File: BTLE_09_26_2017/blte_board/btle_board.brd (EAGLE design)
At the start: 45.7 x 43.2 mm, 15 parts, among them P3 USB-B1HSB6, P4 POWER_JACKPTH, P9 44764-1201

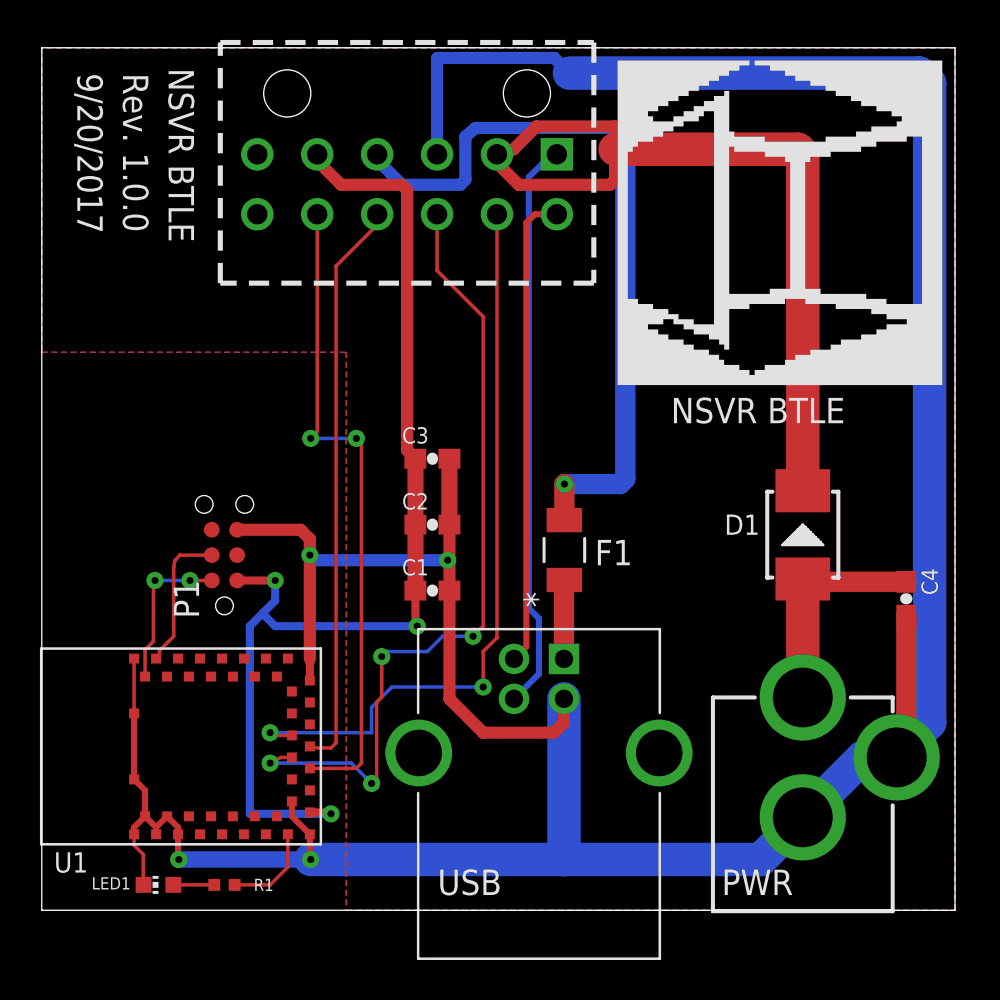
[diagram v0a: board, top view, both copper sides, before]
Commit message: Add Battery & Mounting Holes to BLTE board
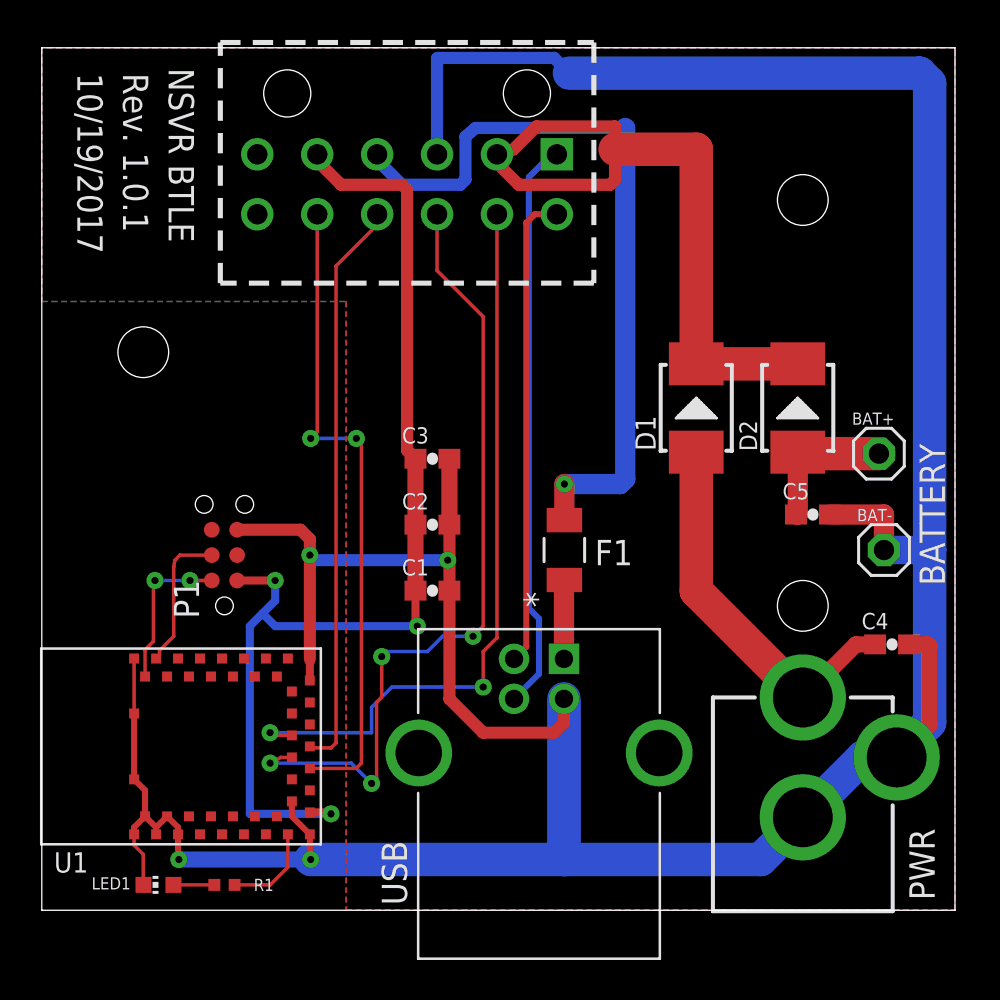
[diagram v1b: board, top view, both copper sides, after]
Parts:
- removed U$4, U$5: (no value), nsvr:NSVR_LOGO
- added BAT+, BAT-: (no value), PatternAgents-ProtoPads:WPAD-1-PTH-2.54
- added C5: 10uF, PatternAgents-ProtoPads:0603-CAP
- added D2: 28V-5A, Seeed-Diode-2016:DO-214AA
- added U$6: (no value), nsvr:NSVR_LOGO
- moved D1 8.29 mm to (32.8, 25.1)
- moved C4 2.39 mm to (42.6, 13.3), turned to 0 degrees
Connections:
- new net VBAT_DC: BAT+.1, C5.1, D2.+
- net GND: now also BAT-.1, C5.2
- net VIN: now also D2.-
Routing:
- net VIN_DC: track 11.2 -> 19.2 mm
- net VBAT_DC: track 0.00 -> 7.35 mm
- net GND: track 175.3 -> 182.1 mm
- net VIN: track 42.3 -> 35.9 mm
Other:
- board text added: "10/19/2017"
- board text added: "BATTERY"
- board text added: "Rev. 1.0.1"
- board text removed: "9/20/2017"
- board text removed: "Rev. 1.0.0"
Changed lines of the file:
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@@
 <wire x1="45.72" y1="43.18" x2="45.72" y2="0" width="0" layer="20"/>
 <wire x1="45.72" y1="0" x2="0" y2="0" width="0" layer="20"/>
-<text x="31.496" y="24.384" size="1.27" layer="21" font="vector" ratio="20">NSVR BTLE</text>
 <text x="6.35" y="42.164" size="1.27" layer="21" font="vector" ratio="20" rot="SR270">NSVR BTLE</text>
-<text x="4.064" y="41.91" size="1.27" layer="21" font="vector" ratio="20" rot="SR270">Rev. 1.0.0</text>
-<text x="1.778" y="41.91" size="1.27" layer="21" font="vector" ratio="20" rot="SR270">9/20/2017</text>
+<text x="4.064" y="41.91" size="1.27" layer="21" font="vector" ratio="20" rot="SR270">Rev. 1.0.1</text>
+<text x="1.778" y="41.91" size="1.27" layer="21" font="vector" ratio="20" rot="SR270">10/19/2017</text>
 <text x="27.686" y="17.272" size="1.27" layer="21" font="vector" ratio="20">F1</text>
-<text x="19.812" y="0.762" size="1.27" layer="21" font="vector" ratio="20">USB</text>
-<text x="34.036" y="0.762" size="1.27" layer="21" font="vector" ratio="20">PWR</text>
+<text x="18.288" y="0.254" size="1.27" layer="21" font="vector" ratio="20" rot="R90">USB</text>
+<text x="44.704" y="0.508" size="1.27" layer="21" font="vector" ratio="20" rot="R90">PWR</text>
+<text x="45.212" y="16.256" size="1.27" layer="21" font="vector" ratio="20" rot="R90">BATTERY</text>
+<hole x="38.1" y="35.56" drill="2.54"/>
+<hole x="5.08" y="27.94" drill="2.54"/>
+<hole x="38.1" y="15.24" drill="2.54"/>
 </plain>
 <attributes>
@@
 <attribute name="PROD_ID" value="CONN-08197" x="78.74" y="-51.308" size="1.778" layer="27" display="off"/>
 </element>
-<element name="C4" library="PatternAgents-ProtoPads" package="0603-CAP" value="10uF" x="43.2816" y="15.5956" rot="R270"/>
+<element name="C4" library="PatternAgents-ProtoPads" package="0603-CAP" value="10uF" x="42.5704" y="13.3096"/>
 <element name="F1" library="1206L050" package="1206LSERIES" value="1206L050YR" x="26.162" y="18.034" smashed="yes" rot="R90">
 <attribute name="COPYRIGHT" value="Copyright C 2015 Accelerated Designs. All rights reserved" x="92.202" y="38.354" size="1.778" layer="27" rot="R90" display="off"/>
@@
 <attribute name="MF" value="On Shore Technology" x="47.752" y="-50.546" size="1.778" layer="27" display="off"/>
 </element>
-<element name="D1" library="Seeed-Diode-2016" package="DO-214AA" value="28V-5A" x="38.1" y="18.796" smashed="yes" rot="R90">
-<attribute name="MPN" value="SS54B" x="38.1" y="18.796" size="1.778" layer="27" rot="R90" display="off"/>
-<attribute name="NAME" x="35.941" y="19.812" size="1.016" layer="25" font="vector" ratio="20" rot="R180"/>
-<attribute name="VALUE" x="40.894" y="17.145" size="0.635" layer="27" ratio="10" rot="R90"/>
-<attribute name="NAME" x="38.1" y="20.066" size="0.5" layer="33" ratio="10" rot="R270"/>
+<element name="D1" library="Seeed-Diode-2016" package="DO-214AA" value="28V-5A" x="32.766" y="25.146" smashed="yes" rot="R90">
+<attribute name="MPN" value="SS54B" x="32.766" y="25.146" size="1.778" layer="27" rot="R90" display="off"/>
+<attribute name="NAME" x="29.718" y="24.765" size="1.016" layer="25" font="vector" ratio="20" rot="R270"/>
+<attribute name="VALUE" x="35.56" y="23.495" size="0.635" layer="27" ratio="10" rot="R90"/>
+<attribute name="NAME" x="32.766" y="26.416" size="0.5" layer="33" ratio="10" rot="R270"/>
 </element>
 <element name="C3" library="PatternAgents-ProtoPads" package="0603-CAP" value="10uF" x="19.558" y="22.606"/>
@@
 <attribute name="NAME" x="10.61" y="1.27" size="0.6096" layer="25" font="vector" ratio="20" align="center-left"/>
 </element>
-<element name="U$4" library="nsvr" package="NSVR_LOGO" value="" x="28.956" y="26.416"/>
-<element name="U$5" library="nsvr" package="NSVR_LOGO" value="" x="44.958" y="26.416" rot="MR0"/>
+<element name="C5" library="PatternAgents-ProtoPads" package="0603-CAP" value="10uF" x="38.608" y="19.812"/>
+<element name="D2" library="Seeed-Diode-2016" package="DO-214AA" value="28V-5A" x="37.846" y="25.146" rot="R90">
+<attribute name="MPN" value="SS54B" x="41.656" y="25.146" size="1.778" layer="27" rot="R90" display="off"/>
+</element>
+<element name="BAT+" library="PatternAgents-ProtoPads" package="WPAD-1-PTH-2.54" value="" x="41.91" y="22.86">
+<attribute name="BOM" value="EXCLUDE" x="41.91" y="22.86" size="1.27" layer="27" ratio="20" display="off"/>
+</element>
+<element name="BAT-" library="PatternAgents-ProtoPads" package="WPAD-1-PTH-2.54" value="" x="42.164" y="18.034">
+<attribute name="BOM" value="EXCLUDE" x="42.164" y="18.034" size="1.27" layer="27" ratio="20" display="off"/>
+</element>
+<element name="U$6" library="nsvr" package="NSVR_LOGO" value="" x="44.958" y="26.67" rot="MR0"/>
 </elements>
 <signals>
@@
 <vertex x="45.72" y="43.18"/>
 <vertex x="0" y="43.18"/>
-<vertex x="0" y="27.94"/>
-<vertex x="15.24" y="27.94"/>
+<vertex x="0" y="30.48"/>
+<vertex x="15.24" y="30.48"/>
 </polygon>
 <polygon width="0.254" layer="16" spacing="0.254" pour="hatch" isolate="0.254" orphans="yes">
@@
 <vertex x="45.72" y="43.18"/>
 <vertex x="0" y="43.18"/>
-<vertex x="0" y="27.94"/>
-<vertex x="15.24" y="27.94"/>
+<vertex x="0" y="30.48"/>
+<vertex x="15.24" y="30.48"/>
 </polygon>
 <wire x1="4.62" y1="6.552" x2="4.62" y2="9.852" width="0.3048" layer="1"/>
@@
 <wire x1="42.8" y1="7.652" x2="42.8" y2="7.748" width="1.6764" layer="16"/>
 <wire x1="42.8" y1="7.748" x2="44.45" y2="9.398" width="1.6764" layer="16"/>
-<wire x1="44.45" y1="9.398" x2="44.45" y2="41.402" width="1.6764" layer="16"/>
+<wire x1="44.45" y1="9.398" x2="44.45" y2="18.034" width="1.6764" layer="16"/>
+<wire x1="44.45" y1="18.034" x2="44.45" y2="41.402" width="1.6764" layer="16"/>
 <wire x1="44.45" y1="41.402" x2="43.942" y2="41.91" width="1.6764" layer="16"/>
 <wire x1="43.942" y1="41.91" x2="26.416" y2="41.91" width="1.6764" layer="16"/>
@@
 <wire x1="26.142" y1="10.584" x2="26.142" y2="2.56" width="1.6764" layer="16"/>
 <wire x1="26.142" y1="2.56" x2="26.162" y2="2.54" width="1.6764" layer="16"/>
-<wire x1="43.2816" y1="14.7456" x2="43.2816" y2="8.1336" width="1.016" layer="1"/>
-<wire x1="43.2816" y1="8.1336" x2="42.8" y2="7.652" width="1.016" layer="1"/>
 <wire x1="20.408" y1="16.002" x2="20.408" y2="10.58" width="0.6096" layer="1"/>
 <wire x1="20.408" y1="10.58" x2="22.098" y2="8.89" width="0.6096" layer="1"/>
@@
 <wire x1="5.08" y1="2.794" x2="5.08" y2="1.282" width="0.1778" layer="1"/>
 <wire x1="5.08" y1="1.282" x2="5.092" y2="1.27" width="0.1778" layer="1"/>
+<contactref element="C5" pad="2"/>
+<contactref element="BAT-" pad="1"/>
+<wire x1="39.458" y1="19.812" x2="42.164" y2="19.812" width="1.016" layer="1"/>
+<wire x1="42.164" y1="19.812" x2="42.164" y2="18.034" width="1.016" layer="1"/>
+<wire x1="43.4204" y1="13.3096" x2="44.3484" y2="13.3096" width="0.8128" layer="1"/>
+<wire x1="44.3484" y1="13.3096" x2="44.45" y2="13.208" width="0.8128" layer="1"/>
+<wire x1="44.45" y1="13.208" x2="44.45" y2="9.302" width="0.8128" layer="1"/>
+<wire x1="44.45" y1="9.302" x2="42.8" y2="7.652" width="0.8128" layer="1"/>
+<wire x1="42.164" y1="18.034" x2="44.45" y2="18.034" width="1.4224" layer="16"/>
 </signal>
 <signal name="RXD_BMD">
@@
 <contactref element="C4" pad="1"/>
 <contactref element="D1" pad="+"/>
-<wire x1="38.1" y1="16.586" x2="38.1" y2="10.652" width="1.6764" layer="1"/>
-<wire x1="43.2816" y1="16.4456" x2="38.2404" y2="16.4456" width="1.016" layer="1"/>
-<wire x1="38.2404" y1="16.4456" x2="38.1" y2="16.586" width="1.016" layer="1"/>
+<wire x1="32.766" y1="22.936" x2="32.766" y2="15.986" width="1.6764" layer="1"/>
+<wire x1="32.766" y1="15.986" x2="38.1" y2="10.652" width="1.6764" layer="1"/>
+<wire x1="41.7204" y1="13.3096" x2="40.7576" y2="13.3096" width="0.8128" layer="1"/>
+<wire x1="40.7576" y1="13.3096" x2="38.1" y2="10.652" width="0.8128" layer="1"/>
 </signal>
 <signal name="3V3_EXT">
@@
 <wire x1="22.86" y1="37.846" x2="22.86" y2="37.338" width="0.6096" layer="1"/>
 <wire x1="22.86" y1="37.338" x2="23.876" y2="36.322" width="0.6096" layer="1"/>
-<wire x1="38.1" y1="21.006" x2="38.1" y2="37.846" width="1.6764" layer="1"/>
-<wire x1="38.1" y1="37.846" x2="37.846" y2="38.1" width="1.6764" layer="1"/>
-<wire x1="37.846" y1="38.1" x2="28.702" y2="38.1" width="1.6764" layer="1"/>
+<wire x1="32.766" y1="27.356" x2="32.766" y2="38.1" width="1.6764" layer="1"/>
+<wire x1="32.766" y1="38.1" x2="28.702" y2="38.1" width="1.6764" layer="1"/>
 <wire x1="28.702" y1="39.243" x2="28.702" y2="38.1" width="0.6096" layer="1"/>
 <wire x1="23.876" y1="36.322" x2="28.448" y2="36.322" width="0.6096" layer="1"/>
@@
 <wire x1="23.622" y1="38.1" x2="23.042" y2="37.846" width="0.6096" layer="1"/>
 <wire x1="23.042" y1="37.846" x2="22.788" y2="37.846" width="0.6096" layer="1"/>
+<contactref element="D2" pad="-"/>
+<wire x1="37.846" y1="27.356" x2="32.766" y2="27.356" width="1.6764" layer="1"/>
 </signal>
 <signal name="I2C_SCL">
@@
 <wire x1="11.43" y1="1.27" x2="9.652" y2="1.27" width="0.1778" layer="1"/>
 </signal>
+<signal name="VBAT_DC">
+<contactref element="C5" pad="1"/>
+<contactref element="D2" pad="+"/>
+<contactref element="BAT+" pad="1"/>
+<wire x1="41.91" y1="22.86" x2="37.846" y2="22.86" width="1.6764" layer="1"/>
+<wire x1="37.846" y1="22.86" x2="37.846" y2="22.936" width="1.6764" layer="1"/>
+<wire x1="37.758" y1="19.812" x2="37.846" y2="19.812" width="1.016" layer="1"/>
+<wire x1="37.846" y1="19.812" x2="37.846" y2="22.936" width="1.016" layer="1"/>
+</signal>
 </signals>
